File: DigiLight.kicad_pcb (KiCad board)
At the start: 2 copper layers, 68 parts, among them IC1 MAX9814 Module, J1 IN_1, J2 IN_2, J4 APU-2, J5 112J-TDAR-R-Micro_SD_Card, J6 WS2811, Q1 BC846, Q2 BC846, Q3 BC846, Q4 IRLML6402, Q5 BC846, SW1 Encoder_Switch, SW2 MENU, U1 LM358, U2 LM358, U3 4066, U4 AMS1117-3.3, U5 ATmega32-16AU, U6 TSOP43xx, Y1 16MHz

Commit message: Refactoring input circuit, reassigned MC pins, replace LCD footprint, create PCB template
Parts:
- removed Q5: BC846, Package_TO_SOT_SMD:SOT-23
- removed R25: 1K, Resistor_SMD:R_1206_3216Metric
- removed R26: 100, Resistor_SMD:R_1206_3216Metric
- removed U6: TSOP43xx, OptoDevice:Vishay_MOLD-3Pin
- added C19: 0.1, Capacitor_SMD:C_1206_3216Metric, F.Cu at (219.8, 54.1)
- added C20: 20, Capacitor_SMD:C_1206_3216Metric, F.Cu at (197.2, 106.2)
- added C21: 100, Capacitor_SMD:C_1206_3216Metric, F.Cu at (181.1, 117.8)
- added C22: 0.1, Capacitor_SMD:C_1206_3216Metric, F.Cu at (281.9, 59.2)
- added C23: 0.1, Capacitor_SMD:C_1206_3216Metric, F.Cu at (225.4, 54.1)
- added C24: 100, Capacitor_SMD:C_1206_3216Metric, F.Cu at (222.5, 57.4)
- added D1: 1N4448W, Diode_SMD:D_SOD-123, F.Cu at (219.8, 44.2)
- added D2: 1N4448W, Diode_SMD:D_SOD-123, F.Cu at (244.4, 25.8)
- added REF**: MountingHole_2.2mm_M2_Pad, MountingHole:MountingHole_2.2mm_M2_Pad, F.Cu at (149.5, 129.8)
- added REF**: MountingHole_2.2mm_M2_Pad, MountingHole:MountingHole_2.2mm_M2_Pad, F.Cu at (238.5, 129.8)
- added REF**: MountingHole_2.2mm_M2_Pad, MountingHole:MountingHole_2.2mm_M2_Pad, F.Cu at (238.5, 81.8)
- added REF**: MountingHole_2.2mm_M2_Pad, MountingHole:MountingHole_2.2mm_M2_Pad, F.Cu at (149.5, 81.8)
- C1: value 470.0 -> 0.1; footprint Capacitor_Tantalum_SMD:CP_EIA-7360-38_Kemet-E_Pad2.25x4.25mm_HandSolder -> Capacitor_SMD:C_1206_3216Metric
- C10: value 0.015 -> 0.1
- C11: value 20 -> 0.1
- C12: value 0.1 -> 100.0; footprint Capacitor_SMD:C_1206_3216Metric -> Capacitor_SMD:CP_Elec_6.3x5.4
- C13: value 20 -> 2.2
- C14: value 0.1 -> 10.0
- C15: value 6800 -> 0.015
- C17: value 100 -> 20
- C18: value 100 -> 6800
- C2: value 1.0 -> 1000.0; footprint Capacitor_SMD:C_1206_3216Metric -> Capacitor_THT:CP_Radial_D8.0mm_P5.00mm
- C3: value 1.0 -> 0.1
- C4, C5: value 100.0 -> 1.0; footprint Capacitor_THT:CP_Radial_D4.0mm_P1.50mm -> Capacitor_SMD:C_1206_3216Metric
- C6, C7: value 2.2 -> 0.1
- C8: value 10.0 -> 1.0
- C9: value 0.1 -> 1000.0; footprint Capacitor_SMD:C_1206_3216Metric -> Capacitor_THT:CP_Radial_D8.0mm_P5.00mm
- IC1, J1, J2, J4, J5, SW1, SW2, Y1: moved to B.Cu
- LCD1: footprint Display:WC1602A -> ExternalLib:WC1602A_4_data
- Q3: value BC846 -> IRLML6402
- Q4: value IRLML6402 -> BC846
- R10: value 15K -> 10K
- R11: value 15K -> 1K
- R12: value 15K -> 2.2K
- R13: value 2.2K -> 10K
- R14: value 2.2K -> 240K
- R15: value 240K -> 9.1K
- R16: value 240K -> 100K
- R17: value 9.1K -> 27K
- R18: value 100K -> 10K
- R19: value 10K -> 1.5K*
- R20: value 27K -> 10K
- R22: value 10K -> 1K
- R24: value 1.5K* -> 100
- R5: value 1.8K -> 1K
- R6: value 1.8K -> 15K
- R7: value 10K -> 15K
- R8: value 1K -> 15K
- U1: value LM358 -> 4066; footprint Package_SO:SOIC-8_3.9x4.9mm_P1.27mm -> Package_SO:SOIC-14_3.9x8.7mm_P1.27mm
- U3: value 4066 -> AMS1117-3.3; footprint Package_SO:SOIC-14_3.9x8.7mm_P1.27mm -> Package_TO_SOT_SMD:SOT-223-3_TabPin2
- U4: value AMS1117-3.3 -> ATmega32-16AU; footprint Package_TO_SOT_SMD:SOT-223-3_TabPin2 -> Package_QFP:TQFP-44_10x10mm_P0.8mm
- U5: value ATmega32-16AU -> TSOP43xx; footprint Package_QFP:TQFP-44_10x10mm_P0.8mm -> OptoDevice:Vishay_MOLD-3Pin; moved to B.Cu
- moved IC1 190.7 mm to (233.0, 124.2)
- moved C2 180.4 mm to (271.8, 59.7)
- moved R11 179.9 mm to (290.4, 53.8)
- moved NT1 177.4 mm to (238.8, 72.4)
- moved C3 176.5 mm to (281.9, 55.9)
- moved R23 173.4 mm to (293.1, 57.1)
- moved U5 166.5 mm to (236.2, 86.5), turned to 270 degrees
- moved C16 166.3 mm to (281.2, 66.2)
- moved R20 158.2 mm to (287.5, 57.1)
- moved R22 157.3 mm to (281.2, 69.4)
- moved R24 154.5 mm to (278.3, 72.7)
- moved R19 153.8 mm to (287.5, 63.7)
- moved J2 150.5 mm to (150.5, 104.2), turned to 90 degrees
- moved Q4 148.2 mm to (292.5, 61.0)
- moved LCD1 146.1 mm to (225.8, 82.0)
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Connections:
- C1 pad 1: Net-(C1-Pad1) -> VPP
- C10 pad 1: Net-(C10-Pad1) -> VDDA
- C11 pad 1: Net-(C11-Pad1) -> VDDA
- C11 pad 2: GND -> GNDA
- C12 pad 1: /RESET -> Net-(C12-Pad1)
- C12 pad 2: GND -> Net-(C12-Pad2)
- C13 pad 2: GND -> Net-(C13-Pad2)
- C14 pad 1: VDDA -> Net-(C14-Pad1)
- C14 pad 2: GNDA -> GND
- C15 pad 1: /AIN -> Net-(C15-Pad1)
- C15 pad 2: Net-(C15-Pad2) -> GNDA
- C16 pad 1: Net-(C16-Pad1) -> VDD
- C16 pad 2: GNDA -> GND
- C17 pad 2: GNDA -> GND
- C18 pad 1: Net-(C18-Pad1) -> /AIN
- C18 pad 2: GND -> Net-(C18-Pad2)
- C2 pad 1: Net-(C2-Pad1) -> Net-(C14-Pad1)
- C2 pad 2: Net-(C2-Pad2) -> GND
- C3 pad 1: Net-(C3-Pad1) -> VDD
- C3 pad 2: Net-(C3-Pad2) -> GND
- C4 pad 1: Net-(C2-Pad1) -> Net-(C4-Pad1)
- C5 pad 1: Net-(C3-Pad1) -> Net-(C5-Pad1)
- C6 pad 1: Net-(C6-Pad1) -> Net-(C14-Pad1)
- C6 pad 2: Net-(C6-Pad2) -> GND
- C7 pad 1: Net-(C7-Pad1) -> VDD
- C7 pad 2: Net-(C7-Pad2) -> GND
- C8 pad 1: Net-(C1-Pad1) -> Net-(C8-Pad1)
- C8 pad 2: GND -> GNDA
- C9 pad 1: VDD -> Net-(C14-Pad1)
- Q1 pad 1: Net-(Q1-Pad1) -> Net-(C8-Pad1)
- Q1 pad 3: Net-(C4-Pad2) -> Net-(C12-Pad2)
- Q2 pad 2: GNDA -> GND
- Q2 pad 3: Net-(C5-Pad2) -> Net-(Q2-Pad3)
- Q3 pad 1: Net-(Q3-Pad1) -> Net-(Q2-Pad3)
- Q3 pad 2: GND -> Net-(C14-Pad1)
- Q3 pad 3: Net-(Q3-Pad3) -> VPP
- Q4 pad 1: Net-(Q3-Pad3) -> Net-(Q4-Pad1)
- Q4 pad 2: Net-(C1-Pad1) -> Net-(J6-Pad2)
- Q4 pad 3: VPP -> /MOSI
- R1 pad 1: Net-(C2-Pad2) -> Net-(C4-Pad2)
- R10 pad 1: Net-(C2-Pad1) -> Net-(C14-Pad1)
- R10 pad 2: GNDA -> Net-(Q2-Pad3)
- R11 pad 1: VDDA -> /PWR_ON
- R11 pad 2: Net-(C3-Pad1) -> Net-(Q2-Pad1)
- R12 pad 1: Net-(C3-Pad1) -> Net-(C13-Pad2)
- R13 pad 1: Net-(C6-Pad2) -> GNDA
- R13 pad 2: GNDA -> Net-(D1-Pad1)
- R14 pad 1: Net-(C7-Pad2) -> Net-(C13-Pad1)
- R14 pad 2: GNDA -> Net-(R14-Pad2)
- R15 pad 1: Net-(R15-Pad1) -> Net-(C15-Pad1)
- R15 pad 2: Net-(C6-Pad1) -> Net-(R15-Pad2)
- R16 pad 1: Net-(R16-Pad1) -> Net-(C18-Pad2)
- R16 pad 2: Net-(C7-Pad1) -> Net-(C15-Pad1)
- R17 pad 1: Net-(C10-Pad1) -> Net-(C21-Pad1)
- R17 pad 2: Net-(R17-Pad2) -> Net-(C18-Pad2)
- R18 pad 1: Net-(C15-Pad2) -> VDD
- R18 pad 2: Net-(C10-Pad1) -> /RESET
- R19 pad 1: VDD -> GND
- R19 pad 2: /RESET -> Net-(LCD1-Pad3)
- R2 pad 1: Net-(C2-Pad2) -> Net-(C4-Pad2)
- R20 pad 1: Net-(C17-Pad1) -> VDD
- R20 pad 2: Net-(C15-Pad2) -> /MISO
- R21 pad 1: GND -> VPP
- R21 pad 2: Net-(LCD1-Pad3) -> Net-(LCD1-Pad15)
- R22 pad 1: VDD -> /WS_LOCK
- R22 pad 2: /MISO -> Net-(Q4-Pad1)
- R23 pad 1: /WS_LOCK -> GND
- R23 pad 2: Net-(Q5-Pad1) -> Net-(J6-Pad2)
- R24 pad 1: VPP -> VDD
- R24 pad 2: Net-(LCD1-Pad15) -> Net-(C24-Pad1)
- R3 pad 1: Net-(Q1-Pad1) -> Net-(C5-Pad2)
- R3 pad 2: /AGC1 -> Net-(J2-Pad2)
- R4 pad 1: Net-(C3-Pad2) -> Net-(C5-Pad2)
- R4 pad 2: Net-(J2-Pad2) -> Net-(J2-Pad5)
- R5 pad 1: Net-(C3-Pad2) -> Net-(C8-Pad1)
- R5 pad 2: Net-(J2-Pad5) -> /AGC
- R6 pad 1: Net-(Q2-Pad1) -> VDDA
- R6 pad 2: /AGC2 -> Net-(C4-Pad1)
- R7 pad 1: Net-(C1-Pad1) -> Net-(C4-Pad1)
- R7 pad 2: Net-(Q3-Pad3) -> GNDA
- R8 pad 1: /PWR_ON -> VDDA
- R8 pad 2: Net-(Q3-Pad1) -> Net-(C5-Pad1)
- R9 pad 1: VDDA -> Net-(C5-Pad1)
- R9 pad 2: Net-(C2-Pad1) -> GNDA
- U1 pad 1: Net-(R15-Pad1) -> Net-(C4-Pad1)
- U1 pad 2: Net-(C6-Pad1) -> Net-(C12-Pad1)
- U1 pad 3: Net-(C2-Pad1) -> Net-(C12-Pad1)
- U1 pad 4: GNDA -> Net-(C5-Pad1)
- U1 pad 5: Net-(C17-Pad1) -> /IN_2_SEL
- U1 pad 6: /AIN -> Net-(D1-Pad1)
- U1 pad 7: /AIN -> GNDA
- U1 pad 8: VDDA -> Net-(R14-Pad2)
- U2 pad 1: Net-(R16-Pad1) -> Net-(R14-Pad2)
- U2 pad 2: Net-(C7-Pad1) -> Net-(C13-Pad1)
- U2 pad 3: Net-(C3-Pad1) -> Net-(C12-Pad1)
- U2 pad 5: (no net) -> Net-(C21-Pad1)
- U2 pad 6: (no net) -> /AIN
- U2 pad 7: (no net) -> /AIN
- U3 pad 1: Net-(R15-Pad1) -> GND
- U3 pad 2: Net-(R17-Pad2) -> VDD
- U3 pad 3: Net-(R17-Pad2) -> Net-(C14-Pad1)
- U4 pad 1: GND -> /MOSI
- U4 pad 2: VDD -> /MISO
- U4 pad 3: Net-(C1-Pad1) -> /SCLK
- U5 pad 1: /MOSI -> /IR
- U5 pad 2: /MISO -> GND
- U5 pad 3: /SCLK -> Net-(C24-Pad1)
- Y1 pad 1: Net-(C11-Pad1) -> Net-(C17-Pad1)
- Y1 pad 2: Net-(C13-Pad1) -> Net-(C20-Pad1)
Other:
- board outline added: 94 x 54 mm

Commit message: Tracing PCB finished
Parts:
- removed the C24 at (222.5, 57.4)
- removed the C7 at (219.8, 47.6)
- added C11: 0.1, Capacitor_SMD:C_1206_3216Metric, F.Cu at (200.2, 104.0)
- added C16: 0.1, Capacitor_SMD:C_1206_3216Metric, F.Cu at (191.2, 74.5)
- added C27: 100, Capacitor_SMD:C_1206_3216Metric, F.Cu at (203.2, 109.2)
- added C6: 1.0, Capacitor_SMD:C_1206_3216Metric, F.Cu at (162.0, 80.0)
- added C8: 0.1, Capacitor_SMD:C_1206_3216Metric, F.Cu at (213.5, 92.0)
- added J3: POWER (5V/3A), ExternalLib:DC-044, B.Cu at (230.5, 64.2)
- C10: renamed from C9; moved to B.Cu
- C12: footprint Capacitor_SMD:CP_Elec_6.3x5.4 -> Capacitor_Tantalum_SMD:CP_EIA-3528-21_Kemet-B_Pad1.50x2.35mm_HandSolder
- C3: renamed from C2; moved to B.Cu
- C4: value 1.0 -> 0.1
- D1, D2: value 1N4448W -> 1N4148WS; footprint Diode_SMD:D_SOD-123 -> Diode_SMD:D_SOD-323
- J6: footprint Connector_JST:JST_XH_B3B-XH-AM_1x03_P2.50mm_Vertical -> Connector_JST:JST_EH_S3B-EH_1x03_P2.50mm_Horizontal; moved to B.Cu
- L1: footprint Inductor_SMD:L_2816_7142Metric -> Inductor_SMD:L_1210_3225Metric
- NT1: moved to B.Cu
- moved D2 104.2 mm to (166.2, 94.8), turned to 180 degrees
- moved C19 97.4 mm to (183.8, 64.0)
- moved C2 95.5 mm to (191.2, 86.0), turned to 270 degrees
- moved C25 93.0 mm to (191.2, 80.0), turned to 90 degrees
- moved R23 86.2 mm to (207.2, 65.0), turned to 90 degrees
- moved R24 86.2 mm to (200.2, 109.2), turned to 270 degrees
- moved Q4 83.3 mm to (209.8, 69.8), turned to 180 degrees
- moved R11 77.9 mm to (213.2, 65.0), turned to 90 degrees
- moved R13 77.8 mm to (168.0, 80.0), turned to 270 degrees
- moved C3 77.1 mm to (194.8, 57.0), turned to 270 degrees
- moved R20 72.3 mm to (221.2, 86.0), turned to 90 degrees
- moved R22 71.1 mm to (210.2, 74.5), turned to 90 degrees
- moved R19 67.1 mm to (221.2, 74.5), turned to 90 degrees
- moved C26 64.7 mm to (206.2, 116.0), turned to 270 degrees
- moved D1 62.5 mm to (172.2, 84.8), turned to 90 degrees
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- renumbered C10 to C13, C11 to C14, C13 to C15, C14 to C17, C15 to C18, C16 to C19, C3 to C2, C17 to C20, C18 to C21, C19 to C22, C20 to C23, C21 to C24, C22 to C25, C23 to C26, C6 to C7, C8 to C9
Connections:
- C4 pad 1: Net-(C4-Pad1) -> VDD
- C4 pad 2: Net-(C4-Pad2) -> GND
- R1 pad 1: Net-(C4-Pad2) -> Net-(C5-Pad2)
- R2 pad 1: Net-(C4-Pad2) -> Net-(C5-Pad2)
- R3 pad 1: Net-(C5-Pad2) -> Net-(C6-Pad2)
- R4 pad 1: Net-(C5-Pad2) -> Net-(C6-Pad2)
- R6 pad 2: Net-(C4-Pad1) -> Net-(C5-Pad1)
- R7 pad 1: Net-(C4-Pad1) -> Net-(C5-Pad1)
- R8 pad 2: Net-(C5-Pad1) -> Net-(C6-Pad1)
- R9 pad 1: Net-(C5-Pad1) -> Net-(C6-Pad1)
- U1 pad 1: Net-(C4-Pad1) -> Net-(C5-Pad1)
- U1 pad 11: Net-(IC1-Pad4) -> Net-(R14-Pad2)
- U1 pad 12: /MC_SEL -> Net-(D1-Pad1)
- U1 pad 4: Net-(C5-Pad1) -> Net-(C6-Pad1)
- U1 pad 6: Net-(D1-Pad1) -> /MC_SEL
- U1 pad 8: Net-(R14-Pad2) -> Net-(IC1-Pad4)
- U4 pad 14: Net-(U4-Pad14) -> /IR
- U4 pad 15: /IR -> /MC_GAIN
- U4 pad 31: /MC_GAIN -> Net-(U4-Pad31)
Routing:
- net VDDA: track 0.00 -> 170.1 mm, vias 0 -> 6
- net /MOSI: track 0.00 -> 126.0 mm, vias 0 -> 4
- net GNDA: track 0.00 -> 119.8 mm, vias 0 -> 10
- net VDD: track 0.00 -> 116.4 mm, vias 0 -> 1
- net /MISO: track 0.00 -> 87.6 mm, vias 0 -> 3
- net /IN_1_SEL: track 0.00 -> 81.3 mm, vias 0 -> 4
- net /SCLK: track 0.00 -> 78.8 mm, vias 0 -> 2
- net GND: track 0.00 -> 73.8 mm, vias 0 -> 17
- net /RESET: track 0.00 -> 71.0 mm, vias 0 -> 2
- net Net-(IC1-Pad4): track 0.00 -> 70.1 mm, vias 0 -> 2
- net /IN_2_SEL: track 0.00 -> 64.1 mm, vias 0 -> 2
- net /MC_SEL: track 0.00 -> 58.7 mm, vias 0 -> 2
- net /SD_CS: track 0.00 -> 52.2 mm, vias 0 -> 1
- net /ENC_BTN: track 0.00 -> 50.5 mm
- net /ENC_UP: track 0.00 -> 41.6 mm
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- added copper zone on B.Cu, net GND
- added copper zone on F.Cu, net GND
- added copper zone on B.Cu, net GNDA
- added copper zone on F.Cu, net GNDA
- added copper zone on F.Cu, net Net-(C10-Pad1)
- added copper zone on F.Cu, net VDD
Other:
- board size 94 x 54 mm -> 95 x 76 mm

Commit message: Final trace
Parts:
- added REF**: DigiLight, ExternalLib:DigiLight, B.Cu at (193.2, 121.8)
- moved REF** 6.00 mm to (150.0, 121.0)
- moved REF** 6.00 mm to (239.0, 121.0)
- moved J5 3.75 mm to (230.2, 85.5)
- moved SW2 2.80 mm to (183.3, 115.5)
- moved J3 1.75 mm to (230.6, 62.5)
- moved J4 0.75 mm to (237.2, 105.5)
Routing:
- net /MISO: track 87.6 -> 91.0 mm
- net /SCLK: track 78.8 -> 82.1 mm
- net VDD: track 116.4 -> 119.5 mm
- net /MENU_BTN: track 30.1 -> 27.3 mm
- net /MOSI: track 126.0 -> 128.0 mm
- net /SD_CS: track 52.2 -> 53.8 mm
- net GND: vias 17 -> 20
- net (no net): vias 6 -> 0
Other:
- board size 95 x 76 mm -> 95 x 70 mm

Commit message: Update models, pcb build finish, change output key.
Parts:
- added C28: 2200, Capacitor_SMD:C_1206_3216Metric, F.Cu at (209.1, 74.5)
- C18: value 0.015 -> 0.01
- C21: value 6800 -> 5600
- C24: value 100 -> 1000
- C27: value 100 -> 4.7uF
- R15: value 9.1K -> 4.7K
- R16: value 100K -> 30K
- R17: value 27K -> 10K
- R22: value 1K -> 10K
- moved R21 7.24 mm to (203.0, 64.9)
- moved Q4 5.40 mm to (206.1, 65.8), turned to 90 degrees
- moved R22 1.91 mm to (212.2, 74.5), turned to 270 degrees
- moved R23 1.86 mm to (209.1, 64.9)
- moved R11 1.10 mm to (212.2, 64.9)
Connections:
- Q4 pad 1: Net-(Q4-Pad1) -> Net-(C28-Pad1)
- Q4 pad 2: Net-(J6-Pad2) -> /MOSI
- Q4 pad 3: /MOSI -> Net-(J6-Pad2)
- R22 pad 1: /WS_LOCK -> Net-(C28-Pad1)
- R22 pad 2: Net-(Q4-Pad1) -> /WS_LOCK
- R23 pad 1: GND -> Net-(J6-Pad2)
- R23 pad 2: Net-(J6-Pad2) -> VPP
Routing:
- net Net-(C28-Pad1): track 0.00 -> 10.9 mm
- net Net-(LCD1-Pad15): track 21.3 -> 12.6 mm
- net GND: track 73.8 -> 65.7 mm
- net VPP: track 27.8 -> 34.1 mm
- net Net-(J6-Pad2): track 12.6 -> 17.6 mm
- net /WS_LOCK: track 24.2 -> 28.3 mm
- net Net-(Q4-Pad1): track 2.61 -> 0.00 mm
- net /LCD_D1: track 23.3 -> 21.3 mm
- net /LCD_D2: track 24.4 -> 22.5 mm
- net /LCD_D0: track 23.0 -> 21.4 mm
- net /LCD_D3: track 25.4 -> 23.8 mm
- net /PWR_ON: track 27.6 -> 29.0 mm
- net /LCD_E: track 21.9 -> 23.1 mm
- net Net-(Q2-Pad1): track 2.42 -> 3.55 mm

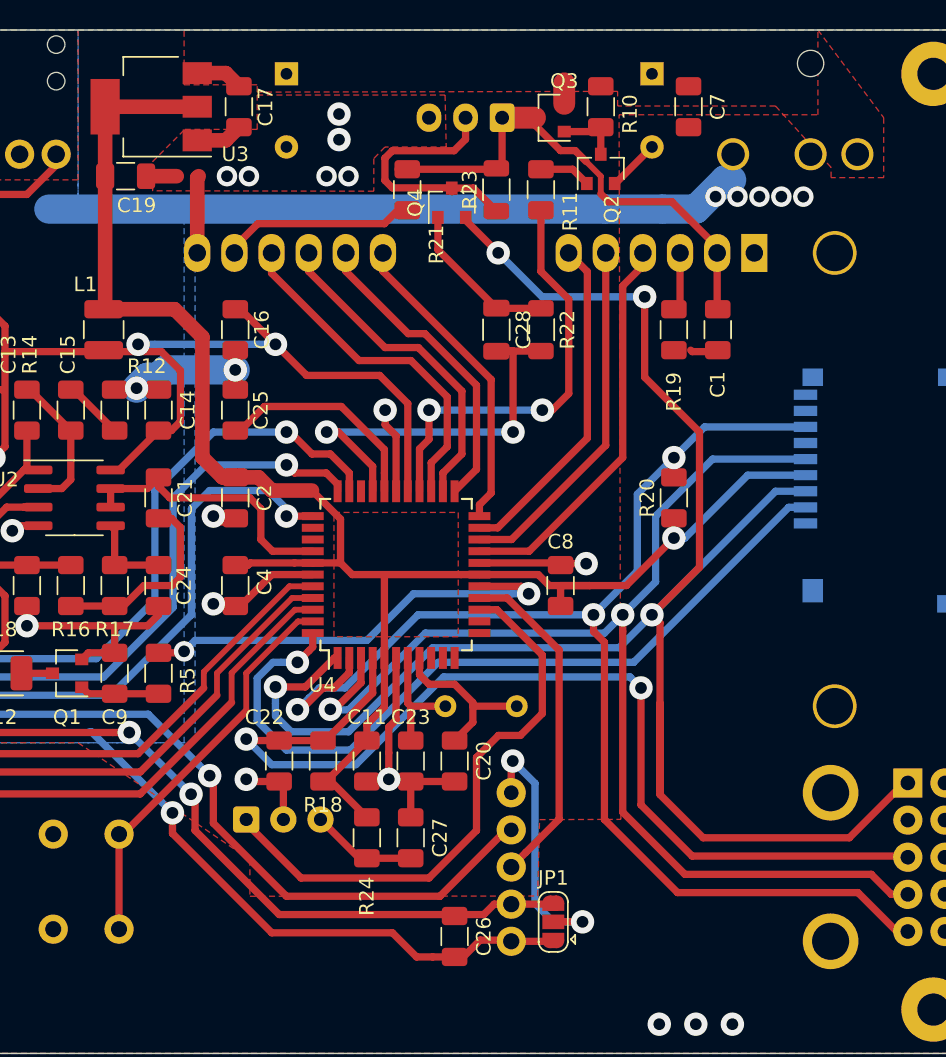
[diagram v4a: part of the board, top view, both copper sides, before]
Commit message: Changed footprint of microphone module, added bias voltage to microphone signal, changed power suply of LCD.
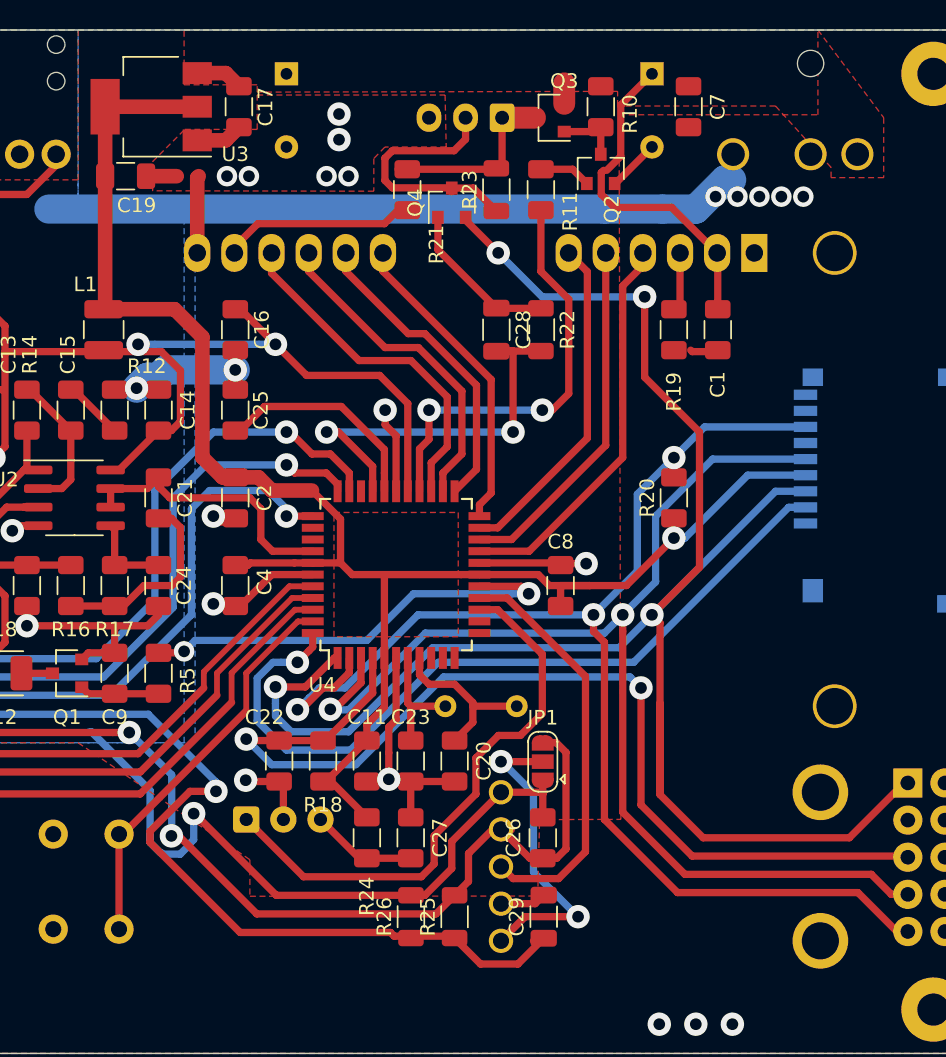
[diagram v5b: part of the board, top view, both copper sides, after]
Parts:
- added C29: 1.0, Capacitor_SMD:C_1206_3216Metric, F.Cu at (212.3, 114.6)
- added R25: 15K, Resistor_SMD:R_1206_3216Metric, F.Cu at (206.2, 114.6)
- added R26: 15K, Resistor_SMD:R_1206_3216Metric, F.Cu at (203.3, 114.6)
- C28: value 2200 -> 1000
- moved JP1 11.0 mm to (212.3, 104.0)
- moved C26 9.05 mm to (212.3, 109.3), turned to 90 degrees
- moved IC1 0.70 mm to (233.3, 111.2)
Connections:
- C1 pad 1: VPP -> +5V
- C10 pad 1: Net-(C10-Pad1) -> +5V
- C17 pad 1: Net-(C10-Pad1) -> +5V
- C3 pad 1: Net-(C10-Pad1) -> +5V
- C7 pad 1: Net-(C10-Pad1) -> +5V
- IC1 pad 4: Net-(IC1-Pad4) -> Net-(C29-Pad2)
- J3 pad 1: Net-(C10-Pad1) -> +5V
- LCD1 pad 2: VPP -> +5V
- Q3 pad 2: Net-(C10-Pad1) -> +5V
- R10 pad 1: Net-(C10-Pad1) -> +5V
- U1 pad 8: Net-(IC1-Pad4) -> Net-(C29-Pad1)
- U3 pad 3: Net-(C10-Pad1) -> +5V
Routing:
- net Net-(C29-Pad1): track 0.00 -> 81.4 mm, vias 0 -> 2
- net Net-(IC1-Pad4): track 70.1 -> 0.00 mm, vias 2 -> 0
- net +5V: track 0.00 -> 28.5 mm
- net VPP: track 34.1 -> 12.5 mm
- net VDDA: track 170.1 -> 184.9 mm
- net GNDA: track 119.8 -> 128.2 mm
- net /MC_GAIN: track 23.1 -> 28.3 mm
- net Net-(C10-Pad1): track 4.83 -> 0.00 mm
- net Net-(C29-Pad2): track 0.00 -> 3.65 mm
- net Net-(IC1-Pad5): track 18.4 -> 21.6 mm
- net /IR: track 39.2 -> 38.7 mm
- added copper zone on F.Cu, net +5V
- removed copper zone on F.Cu, net Net-(C10-Pad1)
